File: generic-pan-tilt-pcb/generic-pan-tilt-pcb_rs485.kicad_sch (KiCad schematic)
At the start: 8 parts, among them U4 ISO1450DW

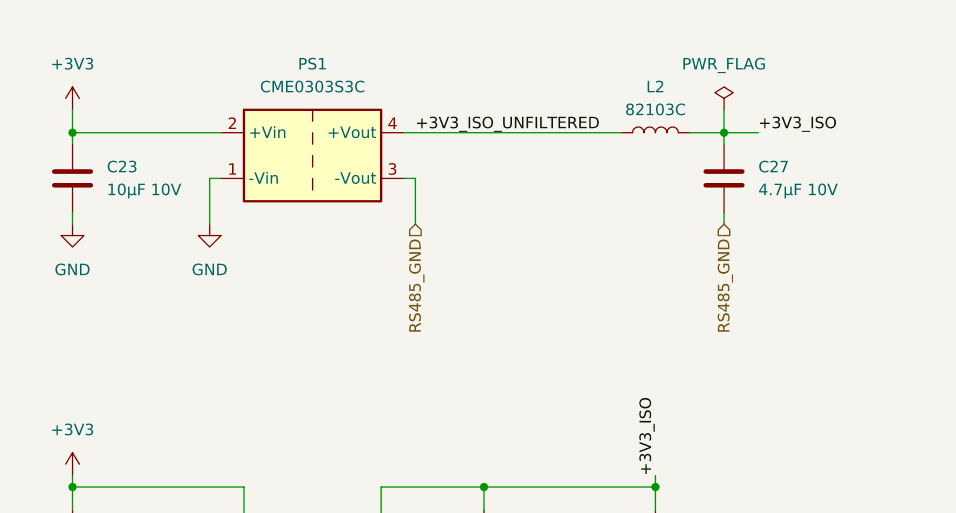
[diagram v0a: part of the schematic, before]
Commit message: fix LED resistors
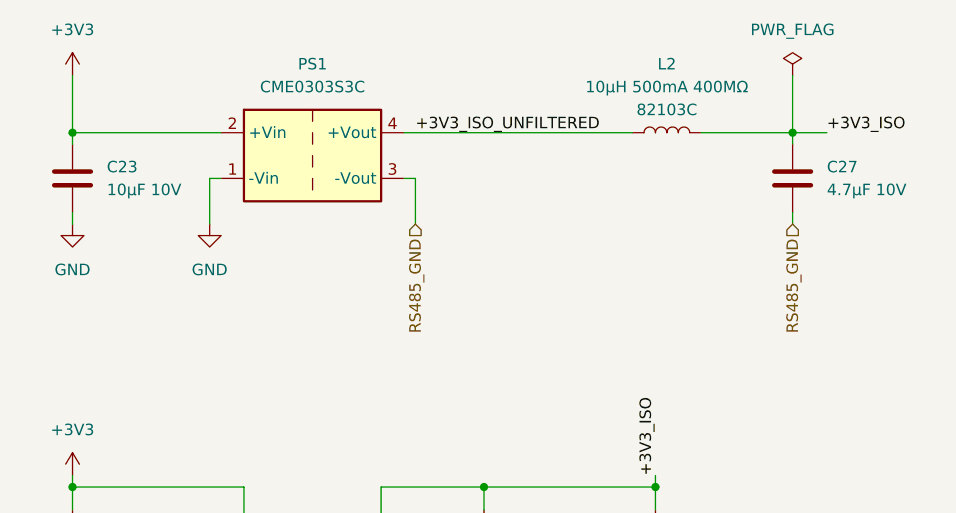
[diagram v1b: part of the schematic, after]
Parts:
- L2: value 82103C -> 10µH 500mA 400MΩ
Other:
- moved on the sheet: C27, L2
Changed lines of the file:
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@@
 	)
 	(junction
-		(at 194.31 31.75)
+		(at 201.93 31.75)
 		(diameter 0)
 		(color 0 0 0 0)
@@
 	(wire
 		(pts
-			(xy 194.31 41.91) (xy 194.31 40.64)
+			(xy 201.93 41.91) (xy 201.93 40.64)
 		)
 		(stroke
@@
 	(wire
 		(pts
-			(xy 182.88 31.75) (xy 158.75 31.75)
-		)
-		(stroke
-			(width 0)
-			(type default)
-		)
-	)
-	(wire
-		(pts
-			(xy 194.31 29.21) (xy 194.31 31.75)
+			(xy 184.15 31.75) (xy 158.75 31.75)
+		)
+		(stroke
+			(width 0)
+			(type default)
+		)
+	)
+	(wire
+		(pts
+			(xy 201.93 25.4) (xy 201.93 31.75)
 		)
 		(stroke
@@
 	(wire
 		(pts
-			(xy 198.12 31.75) (xy 194.31 31.75)
+			(xy 205.74 31.75) (xy 201.93 31.75)
 		)
 		(stroke
@@
 	(wire
 		(pts
-			(xy 194.31 33.02) (xy 194.31 31.75)
+			(xy 191.77 31.75) (xy 201.93 31.75)
+		)
+		(stroke
+			(width 0)
+			(type default)
+		)
+	)
+	(wire
+		(pts
+			(xy 201.93 33.02) (xy 201.93 31.75)
 		)
 		(stroke
@@
 	(wire
 		(pts
-			(xy 194.31 31.75) (xy 190.5 31.75)
-		)
-		(stroke
-			(width 0)
-			(type default)
-		)
-	)
-	(wire
-		(pts
 			(xy 132.08 102.87) (xy 133.35 102.87)
 		)
@@
 	(wire
 		(pts
-			(xy 121.92 29.21) (xy 121.92 31.75)
+			(xy 121.92 25.4) (xy 121.92 31.75)
 		)
 		(stroke
@@
 	)
 	(label "+3V3_ISO"
-		(at 198.12 31.75 0)
+		(at 205.74 31.75 0)
 		(fields_autoplaced yes)
 		(effects
@@
 	(hierarchical_label "RS485_GND"
 		(shape input)
-		(at 194.31 41.91 270)
+		(at 201.93 41.91 270)
 		(fields_autoplaced yes)
 		(effects
@@
 	(symbol
 		(lib_id "power:+3V3")
-		(at 121.92 29.21 0)
+		(at 121.92 25.4 0)
 		(unit 1)
 		(exclude_from_sim no)
@@
 		(fields_autoplaced yes)
 		(property "Reference" "#PWR053"
-			(at 121.92 33.02 0)
+			(at 121.92 29.21 0)
 			(effects
 				(font
@@
 		)
 		(property "Value" "+3V3"
-			(at 121.92 24.13 0)
+			(at 121.92 20.32 0)
 			(effects
 				(font
@@
 		)
 		(property "Footprint" ""
-			(at 121.92 29.21 0)
+			(at 121.92 25.4 0)
 			(effects
 				(font
@@
 		)
 		(property "Datasheet" ""
-			(at 121.92 29.21 0)
+			(at 121.92 25.4 0)
 			(effects
 				(font
@@
 		)
 		(property "Description" "Power symbol creates a global label with name \"+3V3\""
-			(at 121.92 29.21 0)
+			(at 121.92 25.4 0)
 			(effects
 				(font
@@
 	(symbol
 		(lib_id "Device:C")
-		(at 194.31 36.83 0)
+		(at 201.93 36.83 0)
 		(unit 1)
 		(exclude_from_sim no)
@@
 		(fields_autoplaced yes)
 		(property "Reference" "C27"
-			(at 198.12 35.5599 0)
+			(at 205.74 35.5599 0)
 			(effects
 				(font
@@
 		)
 		(property "Value" "4.7μF 10V"
-			(at 198.12 38.0999 0)
+			(at 205.74 38.0999 0)
 			(effects
 				(font
@@
 		)
 		(property "Footprint" "Capacitor_SMD:C_0402_1005Metric"
-			(at 195.2752 40.64 0)
+			(at 202.8952 40.64 0)
 			(effects
 				(font
@@
 		)
 		(property "Datasheet" "~"
-			(at 194.31 36.83 0)
+			(at 201.93 36.83 0)
 			(effects
 				(font
@@
 		)
 		(property "Description" "Unpolarized capacitor"
-			(at 194.31 36.83 0)
+			(at 201.93 36.83 0)
 			(effects
 				(font
@@
 	(symbol
 		(lib_id "power:PWR_FLAG")
-		(at 194.31 29.21 0)
+		(at 201.93 25.4 0)
 		(unit 1)
 		(exclude_from_sim no)
@@
 		(fields_autoplaced yes)
 		(property "Reference" "#FLG05"
-			(at 194.31 27.305 0)
+			(at 201.93 23.495 0)
 			(effects
 				(font
@@
 		)
 		(property "Value" "PWR_FLAG"
-			(at 194.31 24.13 0)
+			(at 201.93 20.32 0)
 			(effects
 				(font
@@
 		)
 		(property "Footprint" ""
-			(at 194.31 29.21 0)
+			(at 201.93 25.4 0)
 			(effects
 				(font
@@
 		)
 		(property "Datasheet" "~"
-			(at 194.31 29.21 0)
+			(at 201.93 25.4 0)
 			(effects
 				(font
@@
 		)
 		(property "Description" "Special symbol for telling ERC where power comes from"
-			(at 194.31 29.21 0)
+			(at 201.93 25.4 0)
 			(effects
 				(font
@@
 	(symbol
 		(lib_id "Device:L")
-		(at 186.69 31.75 90)
+		(at 187.96 31.75 90)
 		(unit 1)
 		(exclude_from_sim no)
@@
 		(on_board yes)
 		(dnp no)
-		(fields_autoplaced yes)
 		(property "Reference" "L2"
-			(at 186.69 26.67 90)
-			(effects
-				(font
-					(size 1.27 1.27)
-				)
-			)
-		)
-		(property "Value" "82103C"
-			(at 186.69 29.21 90)
+			(at 187.96 24.13 90)
+			(effects
+				(font
+					(size 1.27 1.27)
+				)
+			)
+		)
+		(property "Value" "10µH 500mA 400MΩ"
+			(at 187.96 26.67 90)
 			(effects
 				(font
@@
 		)
 		(property "Footprint" "Inductor_SMD:L_1210_3225Metric"
-			(at 186.69 31.75 0)
+			(at 187.96 31.75 0)
 			(effects
 				(font
@@
 		)
 		(property "Datasheet" "~"
-			(at 186.69 31.75 0)
+			(at 187.96 31.75 0)
 			(effects
 				(font
@@
 		)
 		(property "Description" "Inductor"
-			(at 186.69 31.75 0)
+			(at 187.96 31.75 0)
 			(effects
 				(font
@@
 		)
 		(property "digikey#" "811-2473-1-ND"
-			(at 186.69 31.75 0)
+			(at 187.96 31.75 0)
 			(effects
 				(font
@@
 		)
 		(property "manf#" "82103C"
-			(at 186.69 31.75 0)
-			(effects
-				(font
-					(size 1.27 1.27)
-				)
-				(hide yes)
+			(at 187.96 29.21 90)
+			(effects
+				(font
+					(size 1.27 1.27)
+				)
 			)
 		)
 		(property "mouser#" "580-82103C"
-			(at 186.69 31.75 0)
-			(effects
-				(font
+			(at 187.96 31.75 0)
+			(effects
+				(font

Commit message: 0603 caps for psu rs485
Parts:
- C23, C25, C26, C27: footprint Capacitor_SMD:C_0402_1005Metric -> Capacitor_SMD:C_0603_1608Metric
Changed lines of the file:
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@@
 			)
 		)
-		(property "Footprint" "Capacitor_SMD:C_0402_1005Metric"
+		(property "Footprint" "Capacitor_SMD:C_0603_1608Metric"
 			(at 168.6052 81.28 0)
 			(effects
@@
 			)
 		)
-		(property "Footprint" "Capacitor_SMD:C_0402_1005Metric"
+		(property "Footprint" "Capacitor_SMD:C_0603_1608Metric"
 			(at 202.8952 40.64 0)
 			(effects
@@
 			)
 		)
-		(property "Footprint" "Capacitor_SMD:C_0402_1005Metric"
+		(property "Footprint" "Capacitor_SMD:C_0603_1608Metric"
 			(at 187.6552 81.28 0)
 			(effects
@@
 			)
 		)
-		(property "Footprint" "Capacitor_SMD:C_0402_1005Metric"
+		(property "Footprint" "Capacitor_SMD:C_0603_1608Metric"
 			(at 122.8852 40.64 0)
 			(effects

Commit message: fix part numbers, add newark parts, separate fields for part desc
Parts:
- L2: newark# (none) -> 04AJ5966
- PS1: newark# (none) -> 44X7239
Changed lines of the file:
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@@
+			)
+		)
+		(property "newark#" "44X7239"
+			(at 148.59 34.29 0)
+			(effects
+				(font
+					(size 1.27 1.27)
+				)
+				(hide yes)
 			)
 		)
@@
 			(at 187.96 31.75 0)
 			(effects
+				(font
+					(size 1.27 1.27)
+				)
+				(hide yes)
+			)
+		)
+		(property "newark#" "04AJ5966"
+			(at 187.96 31.75 0)
+			(effects

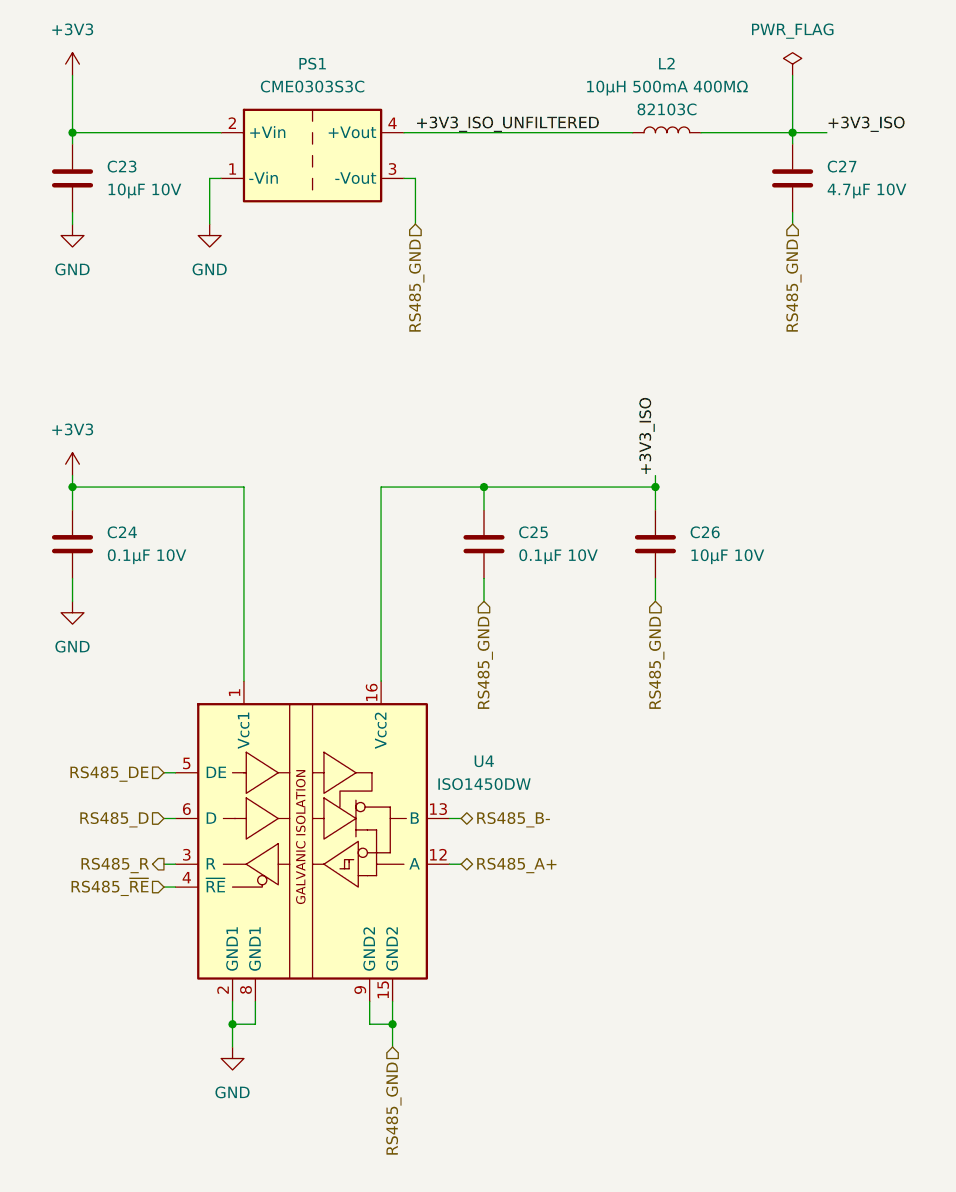
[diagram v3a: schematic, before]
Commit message: main board fix usb, fix uart, all caps and resistors manf and vendor, sch only replace psu and accel caps
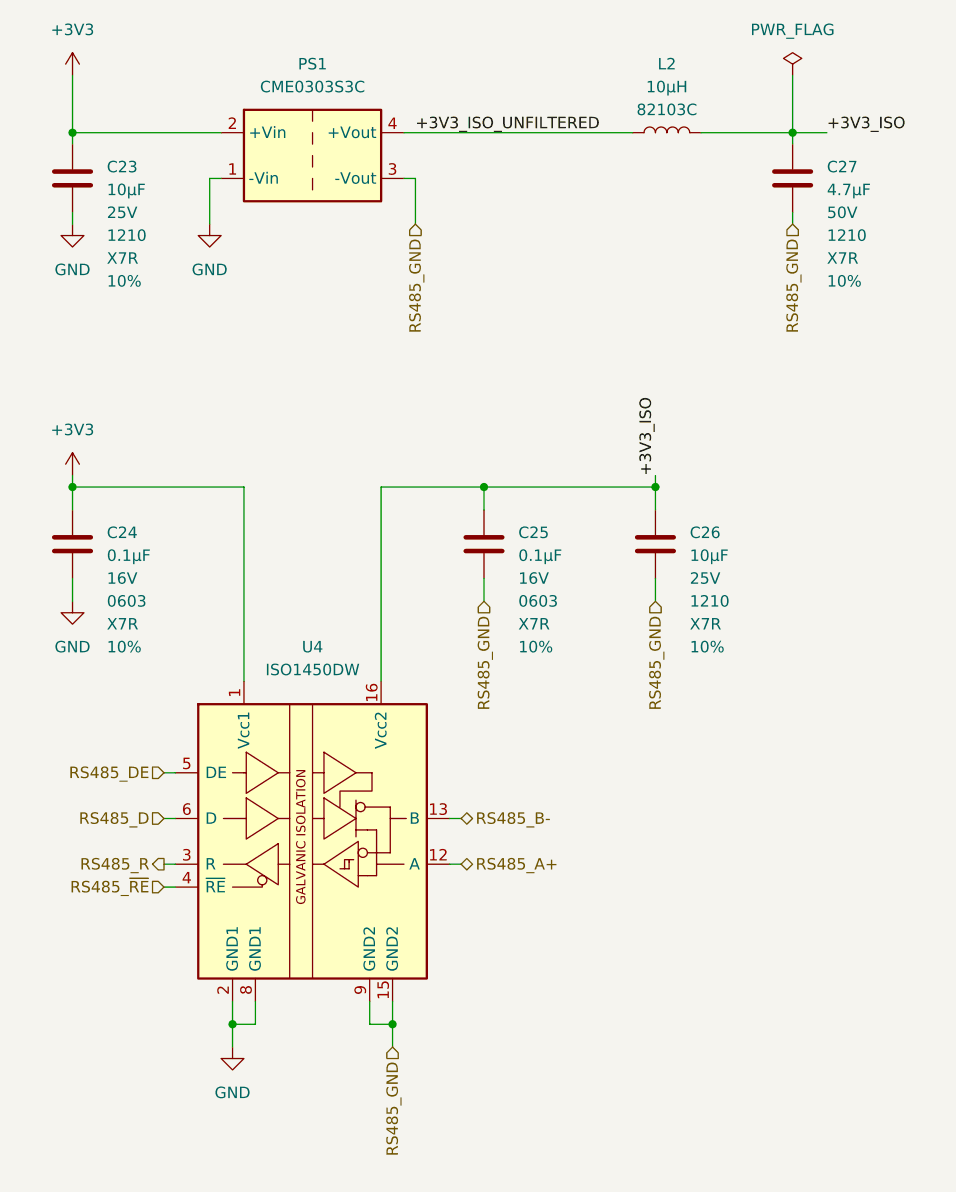
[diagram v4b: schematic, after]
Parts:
- C23, C26: value 10µF 10V -> 10µF; footprint Capacitor_SMD:C_0603_1608Metric -> Capacitor_SMD:C_1210_3225Metric; Case Code (none) -> 1210; Dielectric (none) -> X7R; Tolerance (none) -> 10%; Voltage (none) -> 25V; digikey# (none) -> 1276-1807-1-ND; lcsc# (none) -> C39232; manf# (none) -> CL32B106KAJNNNE; mouser# (none) -> 187-CL32B106KAJNNNE; newark# (none) -> 82AC9529
- C24: value 0.1µF 10V -> 0.1µF; footprint Capacitor_SMD:C_0402_1005Metric -> Capacitor_SMD:C_0603_1608Metric; Case Code (none) -> 0603; Dielectric (none) -> X7R; Tolerance (none) -> 10%; Voltage (none) -> 16V; digikey# (none) -> 1276-1005-1-ND; lcsc# (none) -> C66501; manf# (none) -> CL10B104KO8NNNC; mouser# (none) -> 187-CL10B104KO8NNNC; newark# (none) -> 82AC9325
- C25: value 0.1µF 10V -> 0.1µF; Case Code (none) -> 0603; Dielectric (none) -> X7R; Tolerance (none) -> 10%; Voltage (none) -> 16V; digikey# (none) -> 1276-1005-1-ND; lcsc# (none) -> C66501; manf# (none) -> CL10B104KO8NNNC; mouser# (none) -> 187-CL10B104KO8NNNC; newark# (none) -> 82AC9325
- C27: value 4.7μF 10V -> 4.7μF; footprint Capacitor_SMD:C_0603_1608Metric -> Capacitor_SMD:C_1210_3225Metric; Case Code (none) -> 1210; Dielectric (none) -> X7R; Tolerance (none) -> 10%; Voltage (none) -> 50V; digikey# (none) -> 1276-3343-1-ND; lcsc# (none) -> C2976071; manf# (none) -> CL32B475KBUYNWE; mouser# (none) -> 187-CL32B475KBUYNWE
- L2: value 10µH 500mA 400MΩ -> 10µH; lcsc# (none) -> C492052
- PS1: lcsc# (none) -> C6535309
